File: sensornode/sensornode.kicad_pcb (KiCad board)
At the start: 2 copper layers, 57.6 x 43.9 mm, 24 parts, among them J1 Conn_01x02, J2 Conn_01x06_Male, J3 Conn_01x04_Male, J4 USB_B_Micro, Q1 MMBT3904, U1 ESP-12F, U2 MQ-135, U3 LTC4055, U4 MIC5504-3.3YM5

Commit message: update to latest
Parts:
- added G***: LOGO, logo:diamond, F.Cu at (201.8, 88.2)
- added REF**: MountingHole_3.2mm_M3, MountingHole:MountingHole_3.2mm_M3, F.Cu at (190.8, 62.7)
- added REF**: MountingHole_3.2mm_M3, MountingHole:MountingHole_3.2mm_M3, F.Cu at (190.9, 99.0)
- RV1: footprint Potentiometer_THT:Potentiometer_ACP_CA6-H2,5_Horizontal -> Potentiometer_THT:Potentiometer_Bourns_3266X_Horizontal
- moved R7 11.2 mm to (182.8, 69.1), turned to 180 degrees
- moved R8 10.8 mm to (182.7, 71.3), turned to 180 degrees
- moved J2 6.85 mm to (176.7, 95.0), turned to 55 degrees
- moved C1 1.56 mm to (197.7, 72.2), turned to 300 degrees
- turned RV1 to 210 degrees
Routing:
- net GND: track 157.3 -> 112.1 mm
- net +3V3: track 93.9 -> 84.4 mm, vias 4 -> 3
- net /~RST: track 27.9 -> 20.3 mm
- net Net-(Q1-Pad1): track 4.49 -> 11.9 mm
- net /TX: track 46.4 -> 39.2 mm
- net /GP0: track 49.8 -> 43.8 mm, vias 1 -> 2
- net /RX: track 44.5 -> 38.9 mm
- net +5V: track 55.7 -> 51.5 mm, vias 4 -> 2
- net /mq135_adc: track 50.6 -> 46.7 mm
- net /SDA: track 48.7 -> 45.0 mm
- net VBUS: track 35.3 -> 37.3 mm
- net /SCL: track 51.8 -> 51.2 mm, vias 2 -> 3
- net Net-(C1-Pad1): track 8.59 -> 8.03 mm
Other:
- board text added: "Bobby D"

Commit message: update board
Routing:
- net /~RST: track 20.3 -> 27.8 mm
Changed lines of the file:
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@@
     (thickness 1.6)
     (drawings 7964)
-    (tracks 305)
+    (tracks 309)
     (zones 0)
     (modules 27)
@@
   (page A4)
   (layers
-    (0 F.Cu signal hide)
-    (31 B.Cu signal hide)
+    (0 F.Cu signal)
+    (31 B.Cu signal)
     (32 B.Adhes user)
     (33 F.Adhes user)
@@
       (outputformat 1)
       (mirror false)
-      (drillshape 1)
+      (drillshape 0)
       (scaleselection 1)
       (outputdirectory ""))
@@
   (segment (start 173.408361 92.648362) (end 161.98686 92.648362) (width 0.25) (layer B.Cu) (net 12))
   (segment (start 175.34205 94.58205) (end 173.408361 92.648362) (width 0.25) (layer B.Cu) (net 12))
-  (segment (start 162.2 90.48) (end 162.2 89.73) (width 0.25) (layer F.Cu) (net 13))
   (segment (start 163.42 91.7) (end 162.2 90.48) (width 0.25) (layer F.Cu) (net 13))
   (segment (start 173.675 91.7) (end 163.42 91.7) (width 0.25) (layer F.Cu) (net 13))
@@
   (segment (start 175.11251 92.60001) (end 175.807893 92.60001) (width 0.25) (layer F.Cu) (net 13))
   (segment (start 174.3125 91.8) (end 175.11251 92.60001) (width 0.25) (layer F.Cu) (net 13))
+  (segment (start 162.2 90.48) (end 162.2 89.73) (width 0.25) (layer F.Cu) (net 13))
+  (segment (start 157.025001 91.305001) (end 161.374999 91.305001) (width 0.25) (layer F.Cu) (net 13))
+  (segment (start 156.2 90.48) (end 157.025001 91.305001) (width 0.25) (layer F.Cu) (net 13))
+  (segment (start 161.374999 91.305001) (end 162.2 90.48) (width 0.25) (layer F.Cu) (net 13))
+  (segment (start 156.2 89.73) (end 156.2 90.48) (width 0.25) (layer F.Cu) (net 13))
   (segment (start 158.1 87.7) (end 157.4 87) (width 0.25) (layer B.Cu) (net 14))
   (via (at 164.2 77.4) (size 0.8) (drill 0.4) (layers F.Cu B.Cu) (net 14))

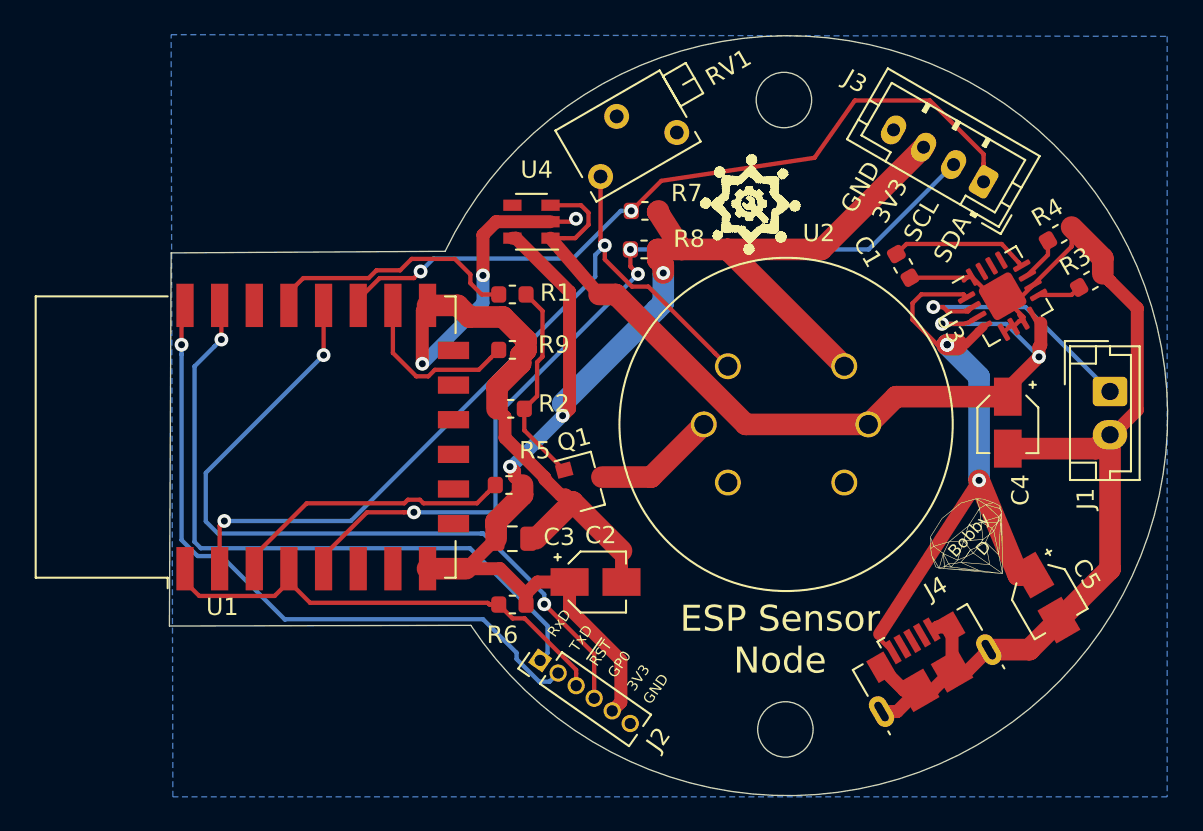
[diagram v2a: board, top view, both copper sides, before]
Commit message: add c6, relayout
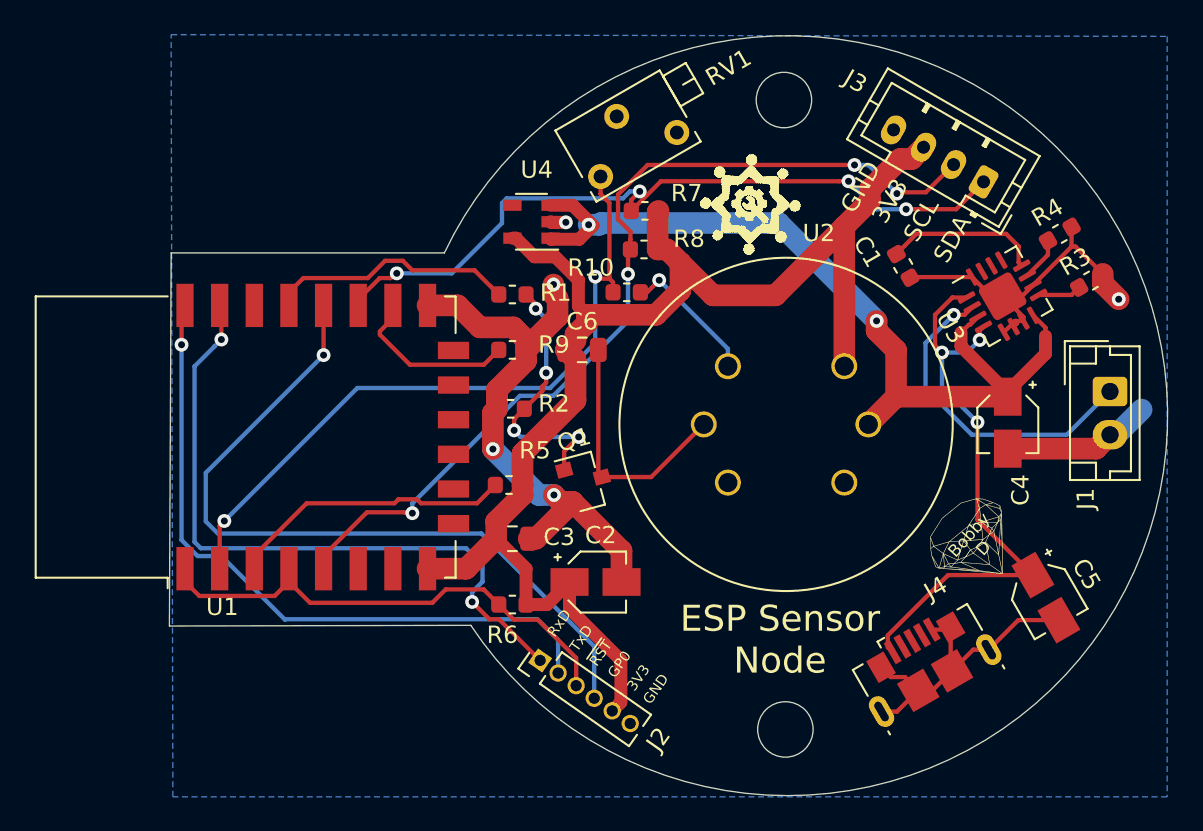
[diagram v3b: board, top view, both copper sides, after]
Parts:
- added C6: 10u ceramic, Capacitor_SMD:C_0805_2012Metric, F.Cu at (179.1, 77.1)
- added R10: 1k8, Resistor_SMD:R_0603_1608Metric, F.Cu at (181.7, 73.8)
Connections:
- J4 pad 2: (no net) -> Net-(J4-Pad2)
- J4 pad 3: (no net) -> Net-(J4-Pad3)
- J4 pad 4: (no net) -> Net-(J4-Pad4)
- U1 pad 10: (no net) -> Net-(U1-Pad10)
- U1 pad 11: (no net) -> Net-(U1-Pad11)
- U1 pad 12: (no net) -> Net-(U1-Pad12)
- U1 pad 13: (no net) -> Net-(U1-Pad13)
- U1 pad 14: (no net) -> Net-(U1-Pad14)
- U1 pad 20: (no net) -> Net-(U1-Pad20)
- U1 pad 6: (no net) -> Net-(U1-Pad6)
- U1 pad 7: (no net) -> Net-(U1-Pad7)
- U1 pad 9: (no net) -> Net-(U1-Pad9)
- U2 pad 3: (no net) -> Net-(U2-Pad3)
- U2 pad 5: (no net) -> Net-(U2-Pad5)
- U2 pad 7: /mq135_adc -> Net-(R10-Pad2)
- U3 pad 13: (no net) -> Net-(U3-Pad13)
- U3 pad 14: (no net) -> Net-(U3-Pad14)
- U3 pad 15: (no net) -> Net-(U3-Pad15)
- U4 pad 4: (no net) -> Net-(U4-Pad4)
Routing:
- net GND: track 112.1 -> 81.9 mm, vias 3 -> 5
- net Net-(R10-Pad2): track 0.00 -> 7.99 mm, vias 0 -> 1
- net Net-(C6-Pad2): track 7.14 -> 14.6 mm
- net /mq135_adc: track 46.7 -> 40.2 mm
- net Net-(J1-Pad1): track 14.7 -> 19.0 mm
- net VBUS: track 37.3 -> 33.5 mm
- net Net-(Q1-Pad1): track 11.9 -> 15.3 mm, vias 0 -> 4
- net +3V3: track 84.4 -> 82.0 mm, vias 3 -> 0
- net /SCL: track 51.2 -> 53.4 mm, vias 3 -> 4
- net /SDA: track 45.0 -> 43.5 mm, vias 2 -> 4
- net +5V: track 51.5 -> 50.1 mm
- net /~RST: track 27.8 -> 28.8 mm
- net Net-(C1-Pad1): track 8.03 -> 9.03 mm
- net /RX: track 38.9 -> 39.2 mm, vias 1 -> 2
- net /GP0: track 43.8 -> 43.7 mm, vias 2 -> 1
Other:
- outline, holes or cut-outs redrawn

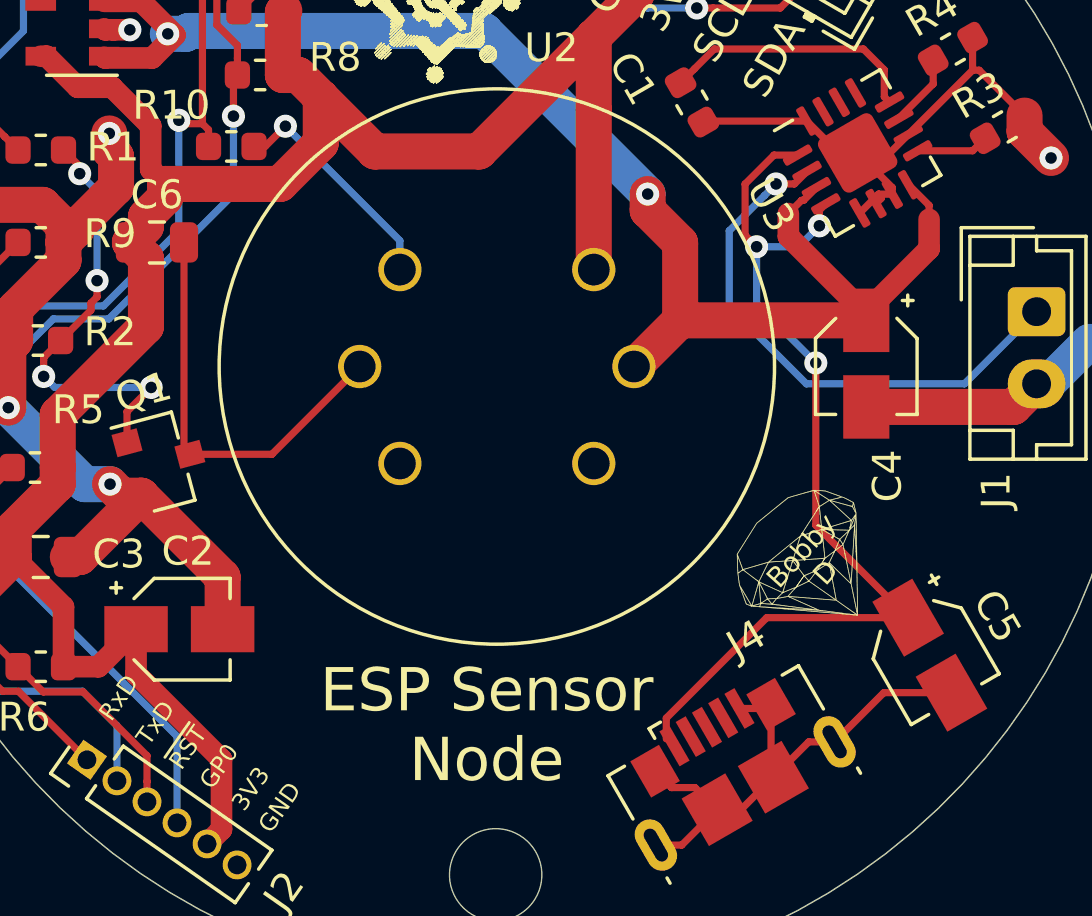
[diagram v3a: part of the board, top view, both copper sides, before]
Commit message: make vbus .75mm
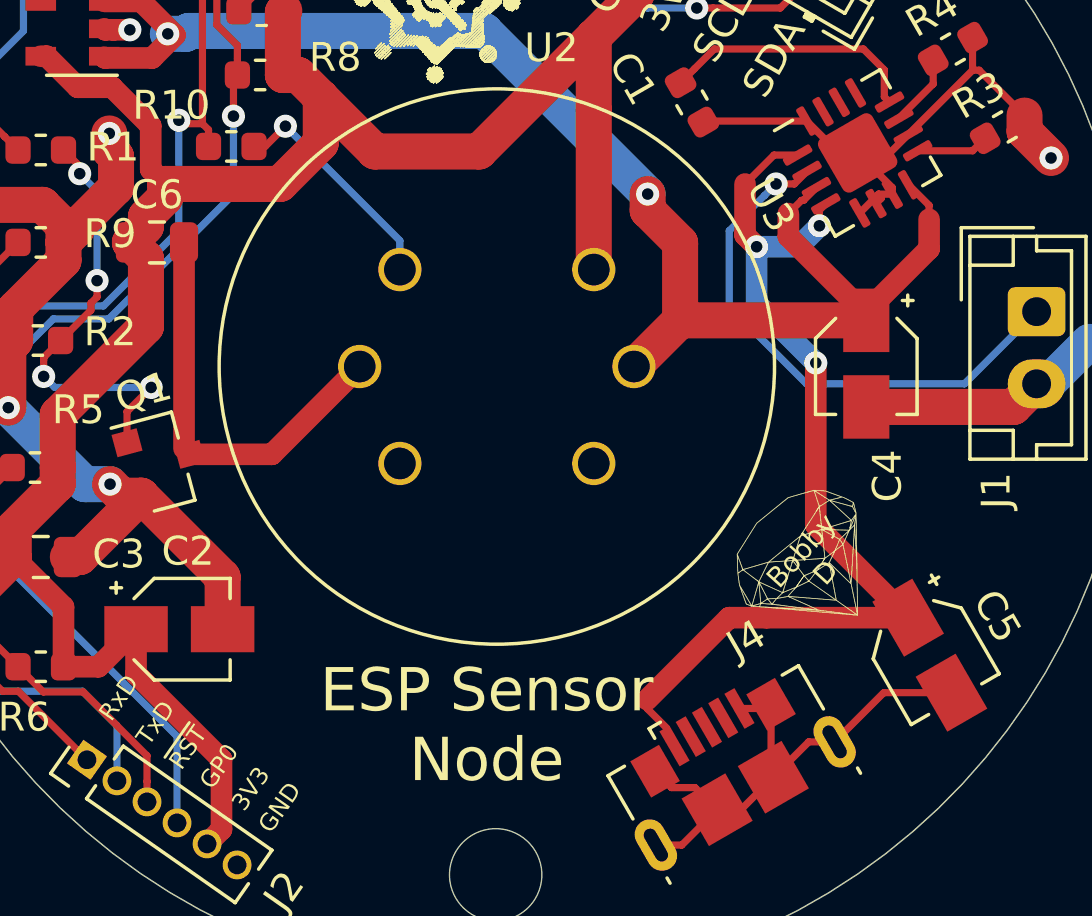
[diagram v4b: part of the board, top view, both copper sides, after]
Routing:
- net VBUS: track 33.5 -> 34.4 mm
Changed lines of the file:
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@@
     (thickness 1.6)
     (drawings 7964)
-    (tracks 351)
+    (tracks 353)
     (zones 0)
     (modules 29)
@@
   (segment (start 202.075 75.984303) (end 202.296178 75.763125) (width 0.25) (layer F.Cu) (net 18))
   (segment (start 202.075 76.525) (end 202.075 75.984303) (width 0.25) (layer F.Cu) (net 18))
-  (segment (start 201.35 77.25) (end 202.075 76.525) (width 0.25) (layer B.Cu) (net 18))
-  (segment (start 199.9 77.25) (end 201.35 77.25) (width 0.25) (layer B.Cu) (net 18))
+  (segment (start 201.35 77.25) (end 202.075 76.525) (width 0.75) (layer B.Cu) (net 18))
+  (segment (start 199.9 77.25) (end 201.35 77.25) (width 0.75) (layer B.Cu) (net 18))
   (via (at 199.9 77.25) (size 0.8) (drill 0.4) (layers F.Cu B.Cu) (net 18))
-  (segment (start 199.500001 76.850001) (end 199.9 77.25) (width 0.25) (layer F.Cu) (net 18))
-  (segment (start 199.500001 75.076997) (end 199.500001 76.850001) (width 0.25) (layer F.Cu) (net 18))
+  (segment (start 199.500001 76.850001) (end 199.9 77.25) (width 0.75) (layer F.Cu) (net 18))
+  (segment (start 199.500001 75.076997) (end 199.500001 76.850001) (width 0.75) (layer F.Cu) (net 18))
   (segment (start 200.502623 74.074375) (end 199.500001 75.076997) (width 0.25) (layer F.Cu) (net 18))
   (segment (start 201.321178 74.074375) (end 200.502623 74.074375) (width 0.25) (layer F.Cu) (net 18))
   (via (at 201.95 81.275) (size 0.8) (drill 0.4) (layers F.Cu B.Cu) (net 18))
-  (segment (start 199.9 77.25) (end 199.9 79.225) (width 0.25) (layer B.Cu) (net 18))
-  (segment (start 199.9 79.225) (end 201.95 81.275) (width 0.25) (layer B.Cu) (net 18))
-  (segment (start 201.95 86.900962) (end 205.15 90.100962) (width 0.25) (layer F.Cu) (net 18))
-  (segment (start 201.95 81.275) (end 201.95 86.900962) (width 0.25) (layer F.Cu) (net 18))
-  (segment (start 196.769689 93.580425) (end 196.769689 94.297578) (width 0.25) (layer F.Cu) (net 18))
-  (segment (start 200.249152 90.100962) (end 196.769689 93.580425) (width 0.25) (layer F.Cu) (net 18))
-  (segment (start 205.15 90.100962) (end 200.249152 90.100962) (width 0.25) (layer F.Cu) (net 18))
+  (segment (start 199.9 77.25) (end 199.9 79.225) (width 0.75) (layer B.Cu) (net 18))
+  (segment (start 199.9 79.225) (end 201.95 81.275) (width 0.75) (layer B.Cu) (net 18))
+  (segment (start 201.95 86.900962) (end 205.15 90.100962) (width 0.75) (layer F.Cu) (net 18))
+  (segment (start 201.95 81.275) (end 201.95 86.900962) (width 0.75) (layer F.Cu) (net 18))
+  (segment (start 205.15 90.100962) (end 200.249152 90.100962) (width 0.75) (layer F.Cu) (net 18))
+  (segment (start 200.249152 90.100962) (end 198.949038 90.100962) (width 0.75) (layer F.Cu) (net 18))
+  (segment (start 198.949038 90.100962) (end 196.11 92.94) (width 0.75) (layer F.Cu) (net 18))
+  (segment (start 196.11 92.94) (end 196.11 93.25) (width 0.25) (layer F.Cu) (net 18))
+  (segment (start 196.11 93.25) (end 196.769689 93.909689) (width 0.25) (layer F.Cu) (net 18))
   (segment (start 175.8875 73.9) (end 176.525021 74.537521) (width 0.25) (layer F.Cu) (net 19))
   (segment (start 176.83751 79.44999) (end 175.7875 80.5) (width 0.25) (layer F.Cu) (net 19))
@@
   (segment (start 177.05 78.990685) (end 176.83751 79.203175) (width 0.25) (layer F.Cu) (net 19))
   (segment (start 177.05 78.425) (end 177.05 78.990685) (width 0.25) (layer F.Cu) (net 19))
-  (segment (start 183.108819 84.441181) (end 186.15 81.4) (width 0.25) (layer F.Cu) (net 20))
-  (segment (start 180.265926 84.441181) (end 183.108819 84.441181) (width 0.25) (layer F.Cu) (net 20))
+  (segment (start 183.108819 84.441181) (end 186.15 81.4) (width 0.75) (layer F.Cu) (net 20))
+  (segment (start 180.265926 84.441181) (end 183.108819 84.441181) (width 0.75) (layer F.Cu) (net 20))
   (segment (start 180.0625 84.237755) (end 180.265926 84.441181) (width 0.25) (layer F.Cu) (net 20))
-  (segment (start 180.0625 77.1) (end 180.0625 84.237755) (width 0.25) (layer F.Cu) (net 20))
+  (segment (start 180.0625 77.1) (end 180.0625 84.237755) (width 0.75) (layer F.Cu) (net 20))
   (via (at 183.575 73.075) (size 0.8) (drill 0.4) (layers F.Cu B.Cu) (net 24))
   (segment (start 182.4875 73.775) (end 182.875 73.775) (width 0.25) (layer F.Cu) (net 24))
